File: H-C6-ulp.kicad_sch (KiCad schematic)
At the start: 76 parts, among them J1 USB_C_Receptacle_USB2.0, J2 AFC24-S24FIC-00, J3 SM02B-SRSS-TB(LF)(SN), J4 SM04B-SRSS-TB_LF__SN_, Q1 Si1308, Q2 Si2301CDS, SW1 SW_Push_Dual, SW2 SW_Push_Dual, U1 ESP32-C6, U2 SGM6029CYG/TR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

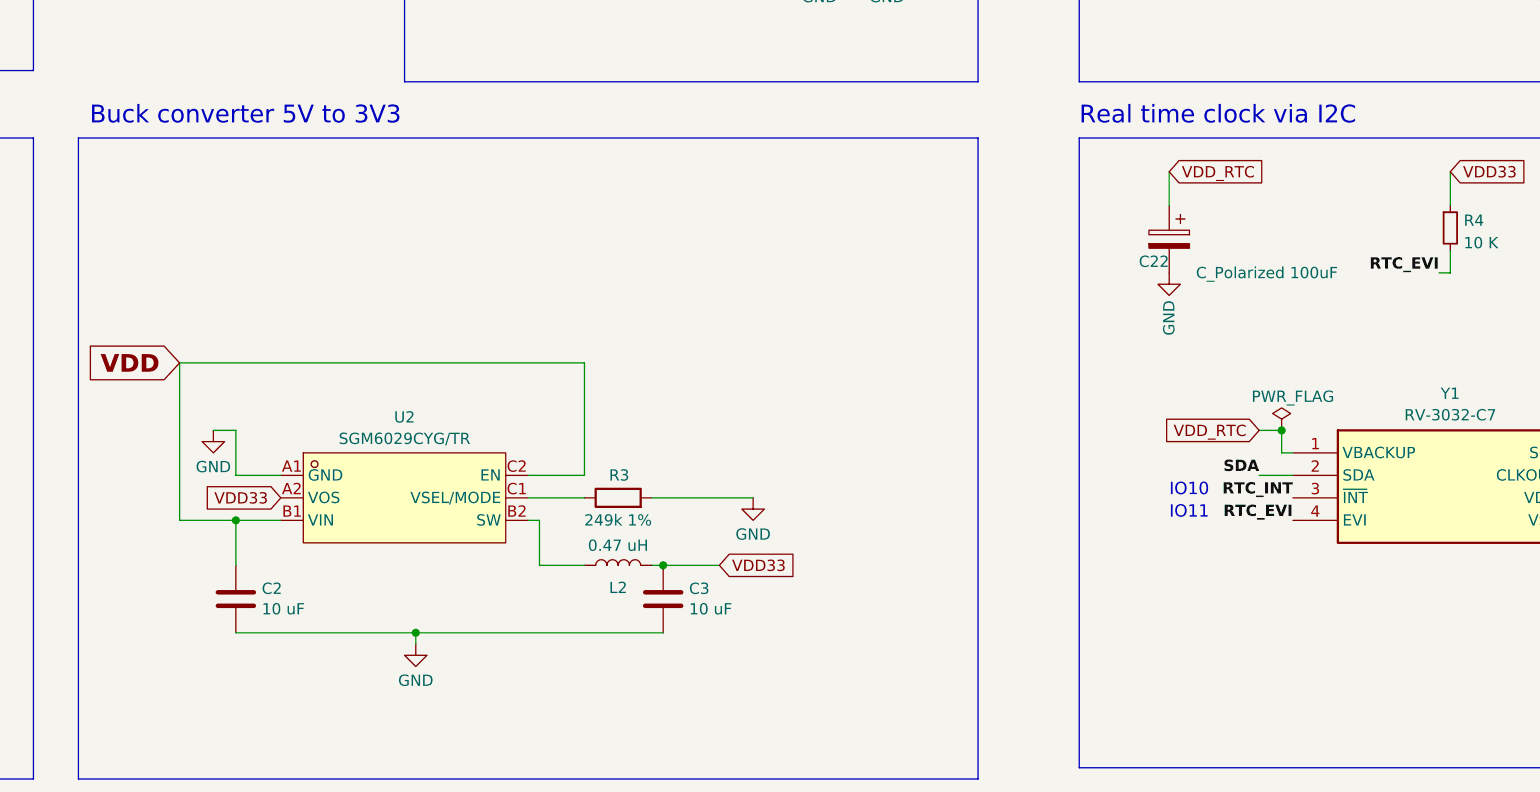
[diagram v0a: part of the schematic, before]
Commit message: Add superCAP as RTC backup
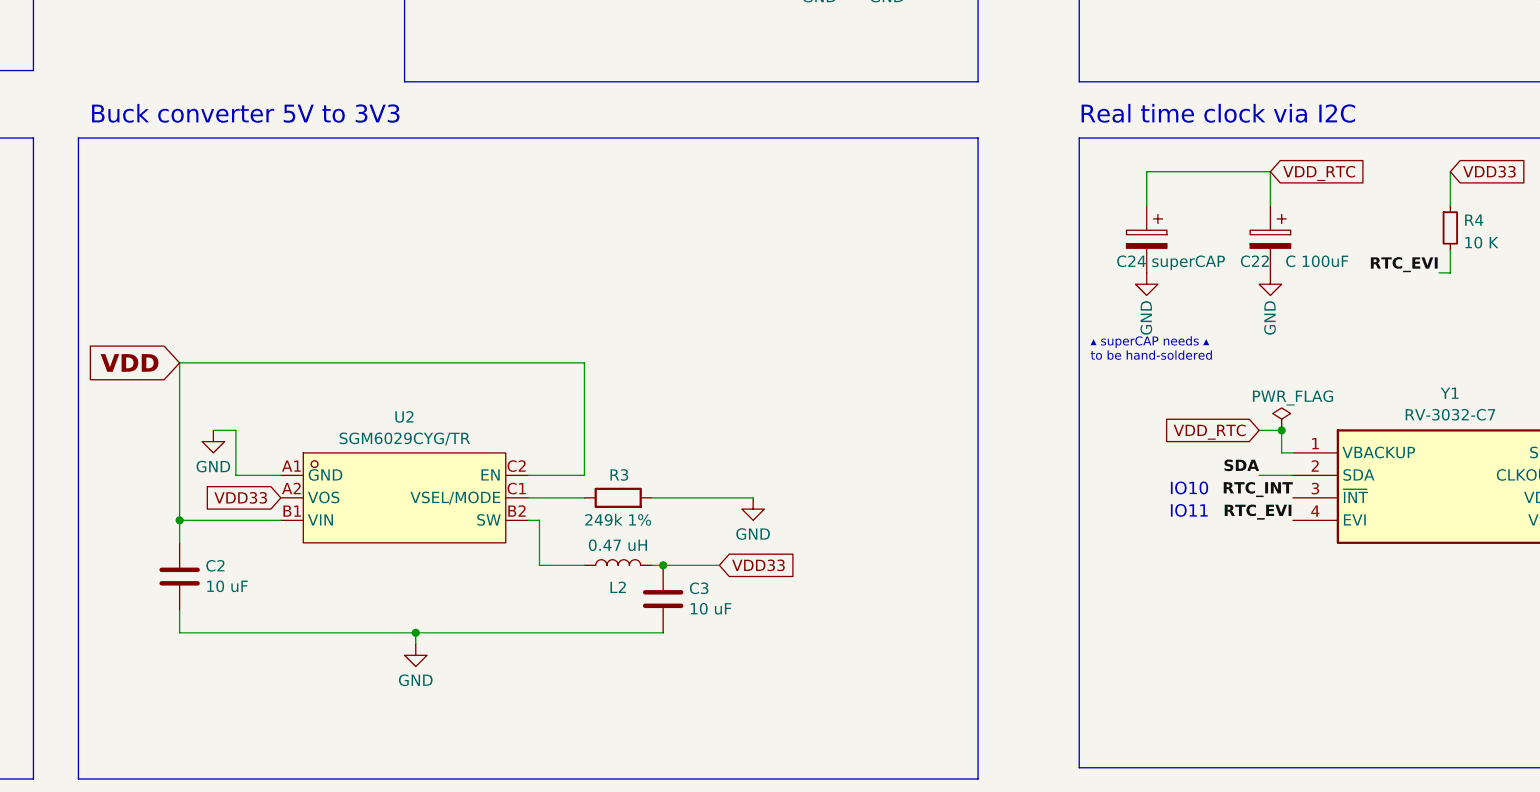
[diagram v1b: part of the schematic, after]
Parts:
- added C24: superCAP, footprints:superCAP-XH414HG, symbol Device:C_Polarized
- C22: value C_Polarized 100uF -> C 100uF
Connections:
- net GND: now also C24.2
- net VDD_RTC: now also C24.1
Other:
- note added: "▴ superCAP needs ▴ to be hand-soldered"
- moved on the sheet: C2, C22
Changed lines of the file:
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@@
   (junction (at 85.09 124.46) (diameter 0) (color 0 0 0 0)
   )
-  (junction (at 96.52 243.84) (diameter 0) (color 0 0 0 0)
+  (junction (at 90.17 243.84) (diameter 0) (color 0 0 0 0)
   )
   (junction (at 161.29 78.74) (diameter 0) (color 0 0 0 0)
@@
     (stroke (width 0) (type default))
   )
+  (wire (pts (xy 199.39 208.28) (xy 199.39 204.47))
+    (stroke (width 0) (type default))
+  )
   (wire (pts (xy 207.01 149.86) (xy 207.01 161.29))
     (stroke (width 0) (type default))
@@
     (stroke (width 0) (type default))
   )
-  (wire (pts (xy 101.6 243.84) (xy 96.52 243.84))
-    (stroke (width 0) (type default))
-  )
-  (wire (pts (xy 96.52 256.54) (xy 116.84 256.54))
+  (wire (pts (xy 90.17 256.54) (xy 116.84 256.54))
     (stroke (width 0) (type default))
   )
@@
     (stroke (width 0) (type default))
   )
-  (wire (pts (xy 201.93 208.28) (xy 201.93 204.47))
+  (wire (pts (xy 213.36 208.28) (xy 213.36 204.47))
     (stroke (width 0) (type default))
   )
@@
     (stroke (width 0) (type default))
   )
+  (wire (pts (xy 199.39 204.47) (xy 213.36 204.47))
+    (stroke (width 0) (type default))
+  )
   (wire (pts (xy 60.96 88.9) (xy 57.15 88.9))
     (stroke (width 0) (type default))
@@
     (stroke (width 0) (type default))
   )
-  (wire (pts (xy 96.52 248.92) (xy 96.52 243.84))
+  (wire (pts (xy 90.17 246.38) (xy 90.17 243.84))
     (stroke (width 0) (type default))
   )
@@
     (stroke (width 0) (type default))
   )
+  (wire (pts (xy 90.17 243.84) (xy 101.6 243.84))
+    (stroke (width 0) (type default))
+  )
   (polyline (pts (xy 290.83 54.61) (xy 290.83 121.92))
     (stroke (width 0) (type default))
@@
     (stroke (width 0) (type default))
   )
+  (wire (pts (xy 90.17 256.54) (xy 90.17 254))
+    (stroke (width 0) (type default))
+  )
   (wire (pts (xy 299.72 80.01) (xy 306.07 80.01))
     (stroke (width 0) (type default))
@@
     (stroke (width 0) (type default))
   )
-  (wire (pts (xy 96.52 243.84) (xy 90.17 243.84))
-    (stroke (width 0) (type default))
-  )
   (wire (pts (xy 158.75 53.34) (xy 147.32 53.34))
     (stroke (width 0) (type default))
@@
     (effects (font (size 2 2)) (justify left bottom))
   )
+  (text "▴ superCAP needs ▴\nto be hand-soldered" (at 193.04 226.06 0)
+    (effects (font (size 1 1) (color 194 0 0 1)) (justify left bottom))
+  )
   (text "IO11" (at 201.93 243.84 0)
     (effects (font (size 1.4 1.4) (color 132 132 132 1)) (justify left bottom))
@@
     )
   )
-  (global_label "VDD_RTC" (shape input) (at 201.93 204.47 0) (fields_autoplaced)
+  (global_label "VDD_RTC" (shape input) (at 213.36 204.47 0) (fields_autoplaced)
     (effects (font (size 1.27 1.27)) (justify left))
-    (property "Intersheetrefs" "${INTERSHEET_REFS}" (at 213.019 204.47 0)
+    (property "Intersheetrefs" "${INTERSHEET_REFS}" (at 224.449 204.47 0)
       (effects (font (size 1.27 1.27)) (justify left) hide)
     )
@@
     )
   )
+  (symbol (lib_id "Device:C_Polarized") (at 199.39 212.09 0) (mirror y) (unit 1)
+    (in_bom yes) (on_board yes) (dnp no)
+    (property "Reference" "C24" (at 199.39 214.63 0)
+      (effects (font (size 1.27 1.27)) (justify left))
+    )
+    (property "Value" "superCAP" (at 208.28 214.63 0)
+      (effects (font (size 1.27 1.27)) (justify left))
+    )
+    (property "Footprint" "footprints:superCAP-XH414HG" (at 198.4248 215.9 0)
+      (effects (font (size 1.27 1.27)) hide)
+    )
+    (property "Datasheet" "https://datasheet.lcsc.com/lcsc/2004141707_KEMET-T491X477K010AT_C513339.pdf" (at 199.39 212.09 0)
+      (effects (font (size 1.27 1.27)) hide)
+    )
+    (property "LCSC" "C129289" (at 199.39 212.09 0)
+      (effects (font (size 1.27 1.27)) hide)
+    )
+    (pin "1")
+    (pin "2")
+    (instances
+      (project "H-C6-ulp"
+        (path "/4820ae53-5724-49d2-a676-459cc31081bd"
+          (reference "C24") (unit 1)
+        )
+      )
+    )
+  )
   (symbol (lib_id "power:GND") (at 219.71 114.3 0) (unit 1)
     (in_bom yes) (on_board yes) (dnp no) (fields_autoplaced)
@@
     )
   )
+  (symbol (lib_id "power:GND") (at 199.39 215.9 0) (unit 1)
+    (in_bom yes) (on_board yes) (dnp no)
+    (property "Reference" "#PWR046" (at 199.39 222.25 0)
+      (effects (font (size 1.27 1.27)) hide)
+    )
+    (property "Value" "GND" (at 199.39 220.98 90)
+      (effects (font (size 1.27 1.27)))
+    )
+    (property "Footprint" "" (at 199.39 215.9 0)
+      (effects (font (size 1.27 1.27)) hide)
+    )
+    (property "Datasheet" "" (at 199.39 215.9 0)
+      (effects (font (size 1.27 1.27)) hide)
+    )
+    (pin "1")
+    (instances
+      (project "H-C6-ulp"
+        (path "/4820ae53-5724-49d2-a676-459cc31081bd"
+          (reference "#PWR046") (unit 1)
+        )
+      )
+    )
+  )
   (symbol (lib_id "Device:R") (at 361.95 111.76 180) (unit 1)
     (in_bom yes) (on_board yes) (dnp no)
@@
     )
   )
-  (symbol (lib_id "power:GND") (at 201.93 215.9 0) (unit 1)
+  (symbol (lib_id "power:GND") (at 213.36 215.9 0) (unit 1)
     (in_bom yes) (on_board yes) (dnp no)
-    (property "Reference" "#PWR011" (at 201.93 222.25 0)
+    (property "Reference" "#PWR011" (at 213.36 222.25 0)
       (effects (font (size 1.27 1.27)) hide)
     )
-    (property "Value" "GND" (at 201.93 220.98 90)
+    (property "Value" "GND" (at 213.36 220.98 90)
       (effects (font (size 1.27 1.27)))
     )
-    (property "Footprint" "" (at 201.93 215.9 0)
+    (property "Footprint" "" (at 213.36 215.9 0)
       (effects (font (size 1.27 1.27)) hide)
     )
-    (property "Datasheet" "" (at 201.93 215.9 0)
+    (property "Datasheet" "" (at 213.36 215.9 0)
       (effects (font (size 1.27 1.27)) hide)
     )
@@
     )
   )
-  (symbol (lib_id "Device:C_Polarized") (at 201.93 212.09 0) (mirror y) (unit 1)
+  (symbol (lib_id "Device:C_Polarized") (at 213.36 212.09 0) (mirror y) (unit 1)
     (in_bom yes) (on_board yes) (dnp no)
-    (property "Reference" "C22" (at 201.93 214.63 0)
+    (property "Reference" "C22" (at 213.36 214.63 0)
       (effects (font (size 1.27 1.27)) (justify left))
     )
-    (property "Value" "C_Polarized 100uF" (at 220.98 215.9 0)
+    (property "Value" "C 100uF" (at 222.25 214.63 0)
       (effects (font (size 1.27 1.27)) (justify left))
     )
-    (property "Footprint" "Capacitor_Tantalum_SMD:CP_EIA-3528-21_Kemet-B" (at 200.9648 215.9 0)
+    (property "Footprint" "Capacitor_Tantalum_SMD:CP_EIA-3528-21_Kemet-B" (at 212.3948 215.9 0)
       (effects (font (size 1.27 1.27)) hide)
     )
-    (property "Datasheet" "https://datasheet.lcsc.com/lcsc/2004141707_KEMET-T491X477K010AT_C513339.pdf" (at 201.93 212.09 0)
+    (property "Datasheet" "https://datasheet.lcsc.com/lcsc/2004141707_KEMET-T491X477K010AT_C513339.pdf" (at 213.36 212.09 0)
       (effects (font (size 1.27 1.27)) hide)
     )
-    (property "LCSC" "C129289" (at 201.93 212.09 0)
+    (property "LCSC" "C129289" (at 213.36 212.09 0)
       (effects (font (size 1.27 1.27)) hide)
     )
@@
     )
   )
-  (symbol (lib_id "Device:C") (at 96.52 252.73 180) (unit 1)
+  (symbol (lib_id "Device:C") (at 90.17 250.19 180) (unit 1)
     (in_bom yes) (on_board yes) (dnp no)
-    (property "Reference" "C2" (at 99.441 251.5616 0)
+    (property "Reference" "C2" (at 93.091 249.0216 0)
       (effects (font (size 1.27 1.27)) (justify right))
     )
-    (property "Value" "10 uF" (at 99.441 253.873 0)
+    (property "Value" "10 uF" (at 93.091 251.333 0)
       (effects (font (size 1.27 1.27)) (justify right))
     )
-    (property "Footprint" "Capacitor_SMD:C_0603_1608Metric" (at 95.5548 248.92 0)
+    (property "Footprint" "Capacitor_SMD:C_0603_1608Metric" (at 89.2048 246.38 0)
       (effects (font (size 1.27 1.27)) hide)
     )
-    (property "Datasheet" "~" (at 96.52 252.73 0)
+    (property "Datasheet" "~" (at 90.17 250.19 0)
       (effects (font (size 1.27 1.27)) hide)
     )
-    (property "LCSC" "C5457064" (at 96.52 252.73 0)
+    (property "LCSC" "C5457064" (at 90.17 250.19 0)
       (effects (font (size 1.27 1.27)) hide)
     )
